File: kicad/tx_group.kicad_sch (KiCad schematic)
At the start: 8 parts, among them U1 74HCT595D, U2 UCC27524DR, U3 UCC27524DR

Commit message: Block-diagram top page, power review fixes, readable sheets
Top level
- Page 1 is now a block diagram of the signal flow (FPGA -> headers ->
  clock buffers / TX drive -> transceivers -> ADCs -> FPGA, mics, power).
- New group sheets hold the reused cells: tx (16 tx_group + 4 en_buf),
  array (64 channel), adcs (8 adc), mics (8 mic), clocks (7 clk_buf).
  Power and headers stay directly under the top. All written by gen_top.py,
  which now also survives a kicad-cli re-save of a cell sheet.

Power (review findings)
- Polyfuse 1812L200/16DR (16 V), TPS65131RGER stated explicitly, input caps
  2 x 10u 1206, 50 V caps on 12 V, inductor values carry minimum Isat.
- +3V3: TLV75733P (ceramic-stable) replaces TLV1117-33.
- New JP5/JP6 isolate +-6V5; every rail: REG node -> jumper -> rail with TP,
  LED (not on analog LDOs) and PWR_FLAG.
- Power sheet is now generated by build_cells.py in a 2x3 block layout
  (build_power.py removed).

Readability and small fixes
- Rails on sideways pins use labelled flags; sideways GND symbols hide text.
- tx_group: 595 outputs wired straight to the drivers.
- Title blocks on every sheet; channel sheet notes and field placement fixed
  (sch_fields.py --only, sch_annotate.py).
- ADC_SDI 10k pull-down, ADC reset/DOUT notes, mic cap 50 V.
- ERC 0 violations, 1,704 parts. PDFs: docs/schematics/00..13.
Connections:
- net BIT1: no longer names the net of U1.15 (QA), U2.2 (INA)
- net BIT2: no longer names the net of U1.1 (QB), U2.4 (INB)
- net BIT3: no longer names the net of U1.2 (QC), U3.2 (INA)
- net BIT4: no longer names the net of U1.3 (QD), U3.4 (INB)
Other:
- company: (none) -> Hybrid 8x8 ultrasonic AESA
- title: (none) -> TX group (x16): 74HCT595 + 2 x UCC27524, 4 elements

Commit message: Optimized, costed BOM with LCSC numbers for every part
scripts/bom.py picks parts (Basic first, stock margin) and writes docs/bom.md,
fab/bom_jlcpcb.csv and scripts/parts.json; sch_lcsc.py fills LCSC fields from it.
Part changes: TPS7A4700RGWT for the out-of-stock TPS7A4701, BAV99 C2500, SS54 in SMA,
SMD1812P200TF16 polyfuse, 600R ferrite, Basic-value +5V/VDRV dividers (VDRV 15.4 V),
Sunlord SWPA6045 footprints, mic 100 nF C0G in 1206. AD7606C-16 and SPH0641 now
assembled by JLCPCB.
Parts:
- C1, C3, C5: LCSC TBD -> C14663
- C2, C4: LCSC TBD -> C28323

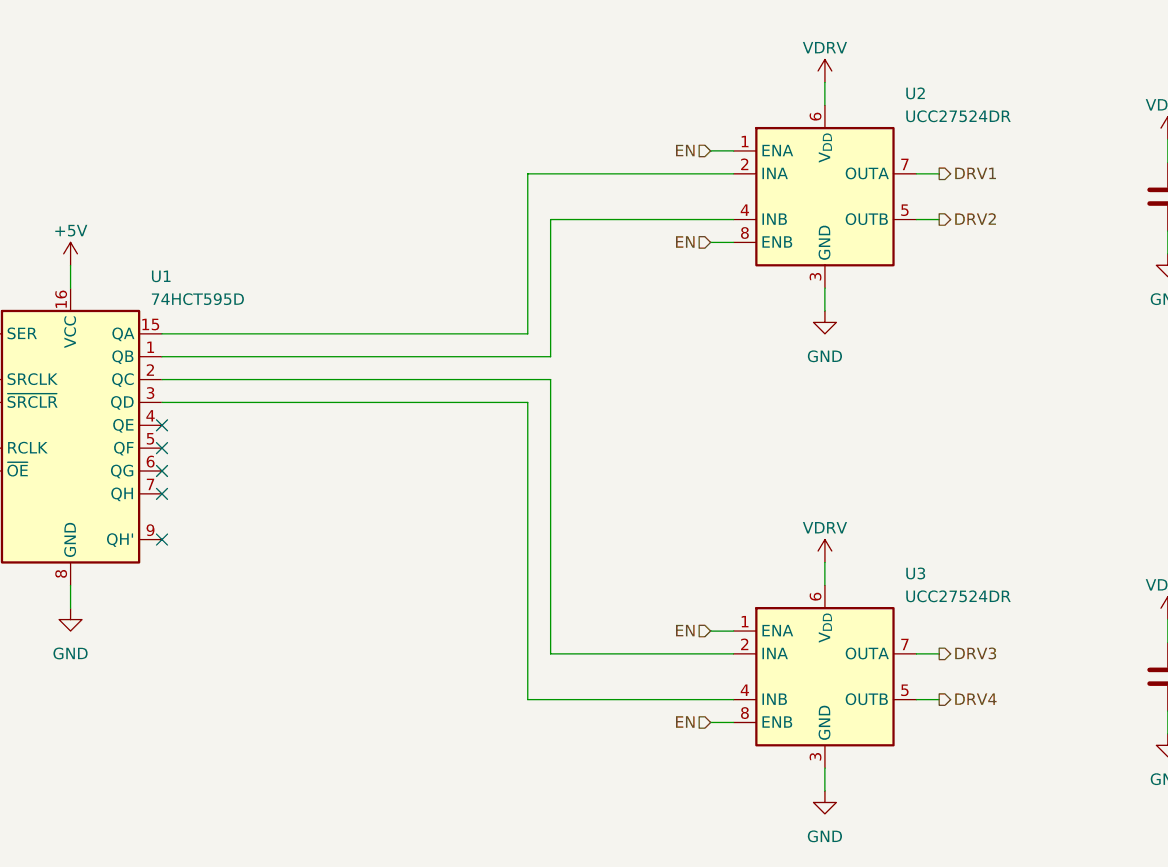
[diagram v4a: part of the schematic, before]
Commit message: Block-first routing: all repeated blocks routed and passing, power input and +-6V5 hand-routed
Schematic
- TX groups and ADC inputs numbered in order (TXG01 = DRV1-4, ADC IN1..4 = RX1..4).
- Power sheets renumbered 1-8 with real references; eFuse RTN no longer tied to GND (TPS2660 9.3.5.5).
- Damped 100 uF bulk caps at the far ends of VIN (C50) and +5V (C51); header clock RC filters removed;
  switch-node snubbers kept as DNP footprints.

Layout and routing
- New routing toolchain: route.py (block stages), block_routes.py (hand-made block routes), maze.py
  (45-degree grid router with rip-up and a per-net time budget), route_lib.py (bend45, chamfer, copper
  checks), block_check.py (DRC and internal nets per block instance), board/cell views.
- Channel, ADC, TX group, clock buffer, enable buffer, mic and header blocks routed and passing
  block_check; no right-angle corners left.
- Designed TX control bus; SDI taps keep 0.7 mm from clock copper.
- Power: 12 V input (eFuse, RTN island, FLT via the front copper) and TPS65131 +-6V5 section with fixed
  templates and hand routing; each power section counts as its own block; the +3V3 LED overflows into
  the gap beside its section.

docs/routing_and_emi.md describes the routing and EMI rules; sim/mic_clock_si adds the mic clock check.
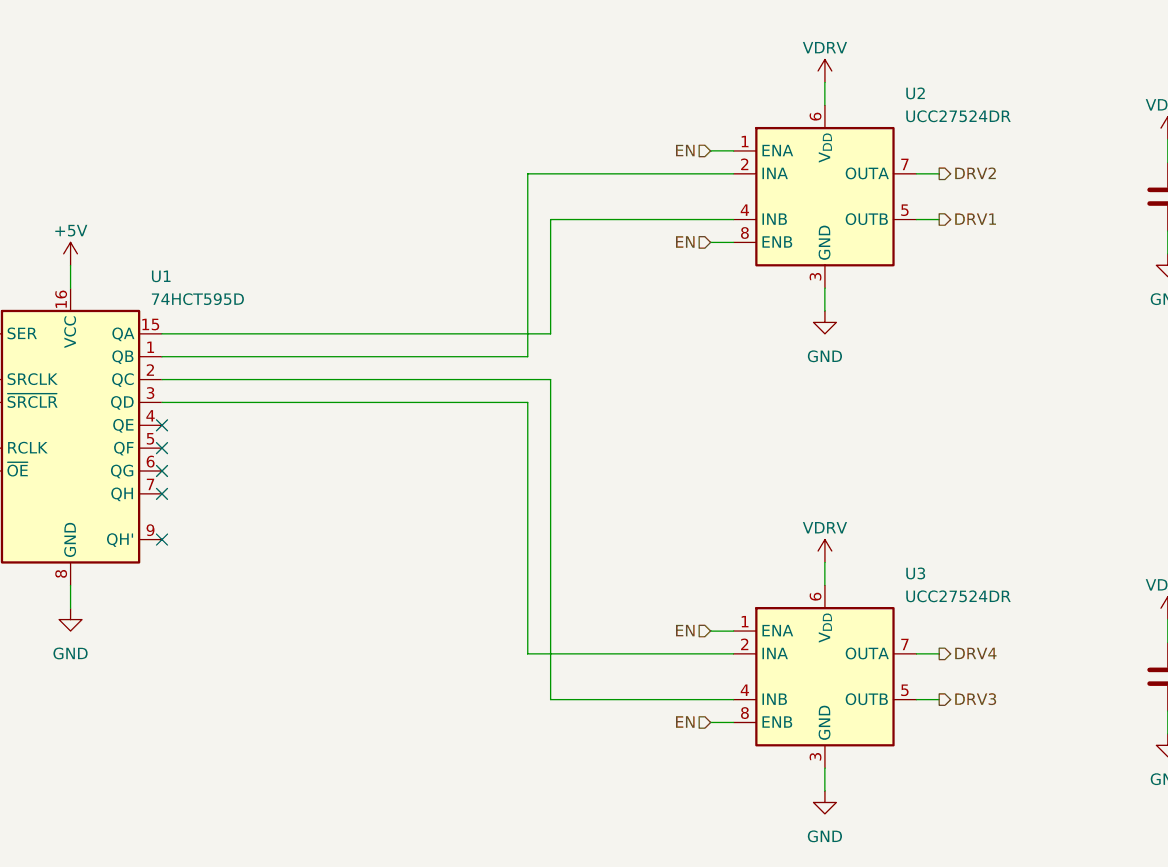
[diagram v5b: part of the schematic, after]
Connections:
- net DRV1: now also U2.5 (OUTB); no longer U2.7 (OUTA)
- net DRV2: now also U2.7 (OUTA); no longer U2.5 (OUTB)
- net DRV3: now also U3.5 (OUTB); no longer U3.7 (OUTA)
- net DRV4: now also U3.7 (OUTA); no longer U3.5 (OUTB)
- net at U1.2 (QC): now also U3.4 (INB); no longer U3.2 (INA)
- net at U1.3 (QD): now also U3.2 (INA); no longer U3.4 (INB)
- net at U2.2 (INA): now also U1.1 (QB); no longer U1.15 (QA)
- net at U2.4 (INB): now also U1.15 (QA); no longer U1.1 (QB)
